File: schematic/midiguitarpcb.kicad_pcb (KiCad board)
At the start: 2 copper layers, 50 x 50 mm, 35 parts, among them CN1 NMJ6HCD2, J1 USB_C_Receptacle_USB2.0_16P, SW1 SW_Omron_B3FS, U1 AMS1117-3.3, U2 DIN-504D-M5, U3 STM32H743ZITx

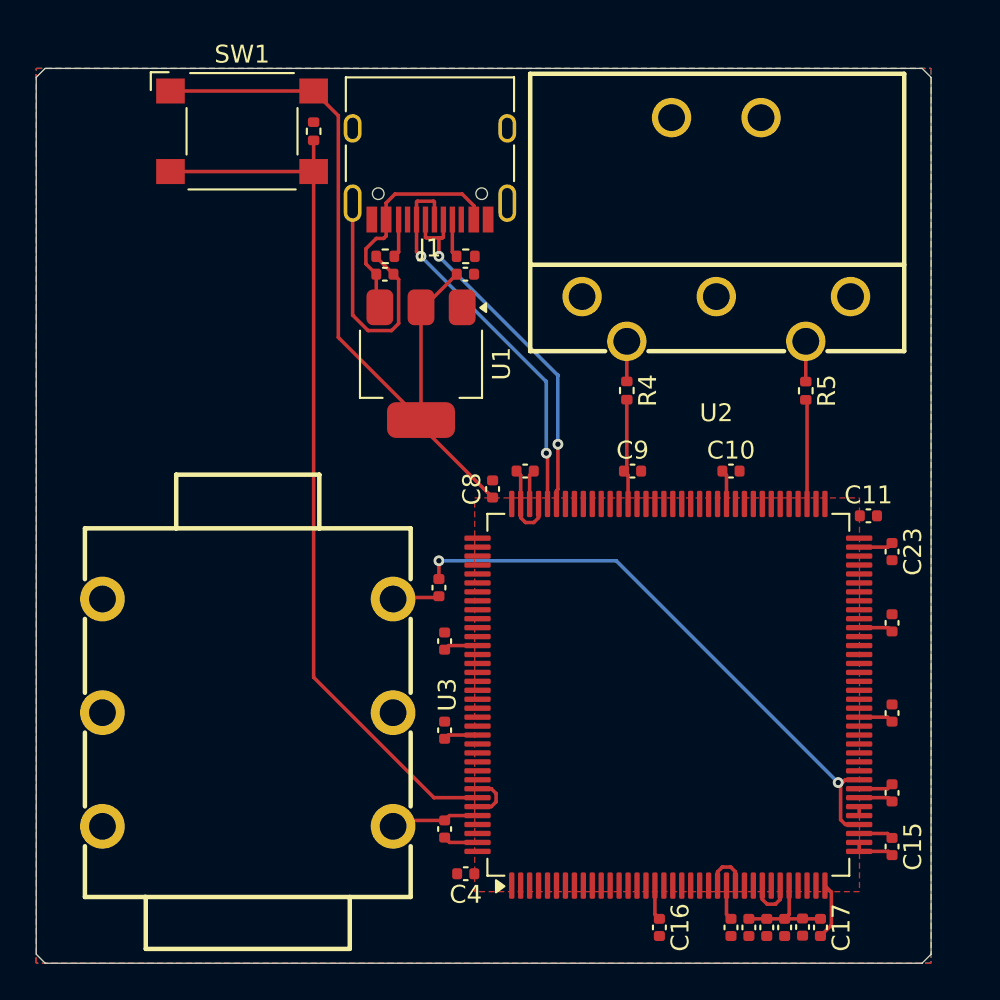
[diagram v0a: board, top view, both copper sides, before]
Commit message: feat(schematic): redo with 2nd opamp
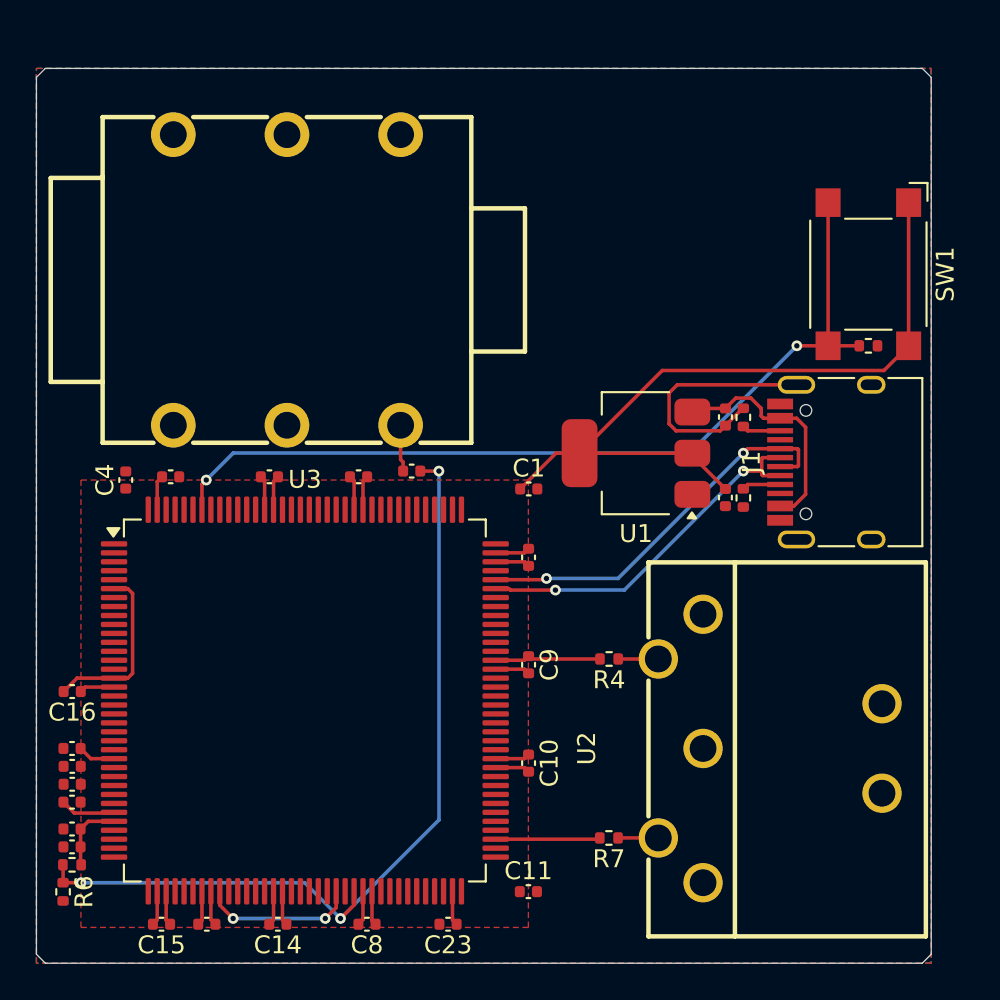
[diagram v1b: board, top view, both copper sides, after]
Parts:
- added R5: 100K, Resistor_SMD:R_0402_1005Metric, F.Cu at (52.0, 94.5)
- added R6: 100K, Resistor_SMD:R_0402_1005Metric, F.Cu at (51.5, 96.0)
- moved C21 42.1 mm to (52.0, 93.5), turned to 180 degrees
- moved C15 41.1 mm to (57.0, 97.8), turned to 180 degrees
- moved C2 40.6 mm to (52.0, 90.0), turned to 180 degrees
- moved C3 39.8 mm to (52.0, 89.0), turned to 180 degrees
- moved C19 39.0 mm to (59.5, 97.8), turned to 0 degrees
- moved C12 38.5 mm to (52.0, 91.0), turned to 180 degrees
- moved C18 38.2 mm to (52.0, 88.0), turned to 180 degrees
- moved C14 36.3 mm to (63.5, 97.8), turned to 180 degrees
- moved SW1 35.9 mm to (96.5, 61.5), turned to -90 degrees
- moved C16 35.4 mm to (52.0, 84.8), turned to 180 degrees
- moved C8 33.8 mm to (68.5, 97.8), turned to 180 degrees
- moved R1 33.2 mm to (96.5, 65.5), turned to 0 degrees
- moved C23 32.4 mm to (73.0, 97.8), turned to 180 degrees
- moved C20 30.2 mm to (52.0, 92.5), turned to 180 degrees
- moved J1 29.4 mm to (95.6, 72.0), turned to 90 degrees
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- renumbered C18 to C12, C19 to C17, C20 to C18, C21 to C19, C8 to C20, C17 to C21, C12 to C8, R5 to R7
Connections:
- C20 pad 1: +3V3 -> Net-(U3-VREF+)
- C21 pad 1: +3V3 -> Net-(U3-VREF+)
- C22 pad 1: Net-(U3-PA4) -> Net-(CN1-T)
- C22 pad 2: Net-(CN1-T) -> Net-(U3-PE9)
- U3 pad 1: GND -> unconnected-(U3-PE2-Pad1)
- U3 pad 10: GND -> unconnected-(U3-PF0-Pad10)
- U3 pad 100: GND -> unconnected-(U3-PA8-Pad100)
- U3 pad 101: GND -> unconnected-(U3-PA9-Pad101)
- U3 pad 102: GND -> unconnected-(U3-PA10-Pad102)
- U3 pad 105: GND -> unconnected-(U3-PA13-Pad105)
- U3 pad 109: GND -> unconnected-(U3-PA14-Pad109)
- U3 pad 11: GND -> unconnected-(U3-PF1-Pad11)
- U3 pad 110: GND -> unconnected-(U3-PA15-Pad110)
- U3 pad 111: GND -> unconnected-(U3-PC10-Pad111)
- U3 pad 112: GND -> unconnected-(U3-PC11-Pad112)
- U3 pad 113: GND -> unconnected-(U3-PC12-Pad113)
- U3 pad 114: GND -> unconnected-(U3-PD0-Pad114)
- U3 pad 115: GND -> unconnected-(U3-PD1-Pad115)
- U3 pad 116: GND -> unconnected-(U3-PD2-Pad116)
- U3 pad 117: GND -> unconnected-(U3-PD3-Pad117)
- U3 pad 118: GND -> unconnected-(U3-PD4-Pad118)
- U3 pad 119: GND -> unconnected-(U3-PD5-Pad119)
- U3 pad 12: GND -> unconnected-(U3-PF2-Pad12)
- U3 pad 122: GND -> unconnected-(U3-PD6-Pad122)
- U3 pad 123: GND -> unconnected-(U3-PD7-Pad123)
- U3 pad 124: GND -> unconnected-(U3-PG9-Pad124)
- U3 pad 125: GND -> unconnected-(U3-PG10-Pad125)
- U3 pad 126: GND -> unconnected-(U3-PG11-Pad126)
- U3 pad 127: GND -> unconnected-(U3-PG12-Pad127)
- U3 pad 128: GND -> unconnected-(U3-PG13-Pad128)
- U3 pad 129: GND -> unconnected-(U3-PG14-Pad129)
- U3 pad 13: GND -> unconnected-(U3-PF3-Pad13)
- U3 pad 132: GND -> unconnected-(U3-PG15-Pad132)
- U3 pad 133: GND -> unconnected-(U3-PB3-Pad133)
- U3 pad 134: GND -> unconnected-(U3-PB4-Pad134)
- U3 pad 135: GND -> unconnected-(U3-PB5-Pad135)
- U3 pad 136: GND -> unconnected-(U3-PB6-Pad136)
- U3 pad 137: GND -> unconnected-(U3-PB7-Pad137)
- U3 pad 139: GND -> unconnected-(U3-PB8-Pad139)
- U3 pad 14: GND -> unconnected-(U3-PF4-Pad14)
- U3 pad 140: GND -> unconnected-(U3-PB9-Pad140)
- U3 pad 141: GND -> unconnected-(U3-PE0-Pad141)
- U3 pad 142: GND -> unconnected-(U3-PE1-Pad142)
- U3 pad 15: GND -> unconnected-(U3-PF5-Pad15)
- U3 pad 18: GND -> unconnected-(U3-PF6-Pad18)
- U3 pad 19: GND -> unconnected-(U3-PF7-Pad19)
- U3 pad 2: GND -> unconnected-(U3-PE3-Pad2)
- U3 pad 20: GND -> unconnected-(U3-PF8-Pad20)
- U3 pad 21: GND -> unconnected-(U3-PF9-Pad21)
- U3 pad 22: GND -> unconnected-(U3-PF10-Pad22)
- U3 pad 23: GND -> unconnected-(U3-PH0-Pad23)
- U3 pad 24: GND -> unconnected-(U3-PH1-Pad24)
- U3 pad 26: GND -> unconnected-(U3-PC0-Pad26)
- U3 pad 27: GND -> unconnected-(U3-PC1-Pad27)
- U3 pad 28: GND -> unconnected-(U3-PC2_C-Pad28)
- U3 pad 29: GND -> unconnected-(U3-PC3_C-Pad29)
- U3 pad 3: GND -> unconnected-(U3-PE4-Pad3)
- U3 pad 32: +3V3 -> Net-(U3-VREF+)
- U3 pad 34: GND -> unconnected-(U3-PA0-Pad34)
- U3 pad 35: GND -> unconnected-(U3-PA1-Pad35)
- U3 pad 36: GND -> unconnected-(U3-PA2-Pad36)
- U3 pad 37: GND -> unconnected-(U3-PA3-Pad37)
- U3 pad 4: GND -> unconnected-(U3-PE5-Pad4)
- U3 pad 40: Net-(U3-PA4) -> unconnected-(U3-PA4-Pad40)
- U3 pad 41: GND -> unconnected-(U3-PA5-Pad41)
- U3 pad 42: GND -> unconnected-(U3-PA6-Pad42)
- U3 pad 45: Net-(U3-PA4) -> Net-(U3-PC5)
- U3 pad 46: GND -> unconnected-(U3-PB0-Pad46)
- U3 pad 47: GND -> unconnected-(U3-PB1-Pad47)
- U3 pad 48: GND -> unconnected-(U3-PB2-Pad48)
- U3 pad 49: GND -> unconnected-(U3-PF11-Pad49)
- U3 pad 5: GND -> unconnected-(U3-PE6-Pad5)
- U3 pad 50: GND -> unconnected-(U3-PF12-Pad50)
- U3 pad 53: GND -> unconnected-(U3-PF13-Pad53)
- U3 pad 54: GND -> unconnected-(U3-PF14-Pad54)
- U3 pad 55: GND -> unconnected-(U3-PF15-Pad55)
- U3 pad 56: GND -> unconnected-(U3-PG0-Pad56)
- U3 pad 57: GND -> unconnected-(U3-PG1-Pad57)
- U3 pad 58: GND -> Net-(U3-PC5)
- U3 pad 59: GND -> unconnected-(U3-PE8-Pad59)
- U3 pad 60: GND -> Net-(U3-PE9)
- U3 pad 63: GND -> unconnected-(U3-PE10-Pad63)
- U3 pad 64: GND -> unconnected-(U3-PE11-Pad64)
- U3 pad 65: GND -> unconnected-(U3-PE12-Pad65)
- U3 pad 66: GND -> unconnected-(U3-PE13-Pad66)
- U3 pad 67: GND -> unconnected-(U3-PE14-Pad67)
- U3 pad 68: GND -> unconnected-(U3-PE15-Pad68)
- U3 pad 69: GND -> unconnected-(U3-PB10-Pad69)
- U3 pad 7: GND -> unconnected-(U3-PC13-Pad7)
- U3 pad 70: GND -> unconnected-(U3-PB11-Pad70)
- U3 pad 73: GND -> unconnected-(U3-PB12-Pad73)
- U3 pad 74: GND -> unconnected-(U3-PB13-Pad74)
- U3 pad 76: GND -> unconnected-(U3-PB15-Pad76)
- U3 pad 77: GND -> unconnected-(U3-PD8-Pad77)
- U3 pad 78: GND -> unconnected-(U3-PD9-Pad78)
- U3 pad 79: GND -> unconnected-(U3-PD10-Pad79)
- U3 pad 8: GND -> unconnected-(U3-PC14-Pad8)
- U3 pad 80: GND -> unconnected-(U3-PD11-Pad80)
- U3 pad 81: GND -> unconnected-(U3-PD12-Pad81)
- U3 pad 82: GND -> unconnected-(U3-PD13-Pad82)
- U3 pad 85: GND -> unconnected-(U3-PD14-Pad85)
- U3 pad 86: GND -> unconnected-(U3-PD15-Pad86)
- U3 pad 87: GND -> unconnected-(U3-PG2-Pad87)
- U3 pad 88: GND -> unconnected-(U3-PG3-Pad88)
- U3 pad 89: GND -> unconnected-(U3-PG4-Pad89)
- U3 pad 9: GND -> unconnected-(U3-PC15-Pad9)
- U3 pad 90: GND -> unconnected-(U3-PG5-Pad90)
- U3 pad 91: GND -> unconnected-(U3-PG6-Pad91)
- U3 pad 92: GND -> unconnected-(U3-PG7-Pad92)
- U3 pad 93: GND -> unconnected-(U3-PG8-Pad93)
- U3 pad 96: GND -> unconnected-(U3-PC6-Pad96)
- U3 pad 97: GND -> unconnected-(U3-PC7-Pad97)
- U3 pad 98: GND -> unconnected-(U3-PC8-Pad98)
- U3 pad 99: GND -> unconnected-(U3-PC9-Pad99)
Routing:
- net Net-(U3-PE9): track 0.00 -> 47.5 mm, vias 0 -> 3
- net Net-(U3-PA4): track 32.7 -> 0.00 mm, vias 2 -> 0
- net Net-(U3-PC5): track 0.00 -> 8.74 mm, vias 0 -> 2
- net +3V3: track 71.4 -> 63.6 mm
- net GND: track 37.7 -> 42.3 mm
- net Net-(U3-VREF+): track 0.00 -> 4.06 mm
- net Net-(U3-BOOT0): track 49.9 -> 49.4 mm, vias 0 -> 2
